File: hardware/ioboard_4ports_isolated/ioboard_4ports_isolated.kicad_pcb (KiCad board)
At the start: 2 copper layers, 106 x 55 mm, 60 parts, among them J1 Conn_02x06_Odd_Even, J10 XLR3, J11 XLR3, J12 Conn_01x03, J13 Conn_01x03, J14 8P8C, J2 XLR3, J3 XLR3, J4 XLR3, J5 XLR3, J6 Conn_01x03, J7 Conn_01x03, J8 XLR3, J9 XLR3, U1 M24C64-RMN6TP, U2 CRE1S0505DC, U3 CRE1S0505DC, U4 ADM2483xRW, U5 ADM2483xRW, U6 ADM2483xRW, U7 ADM2483xRW

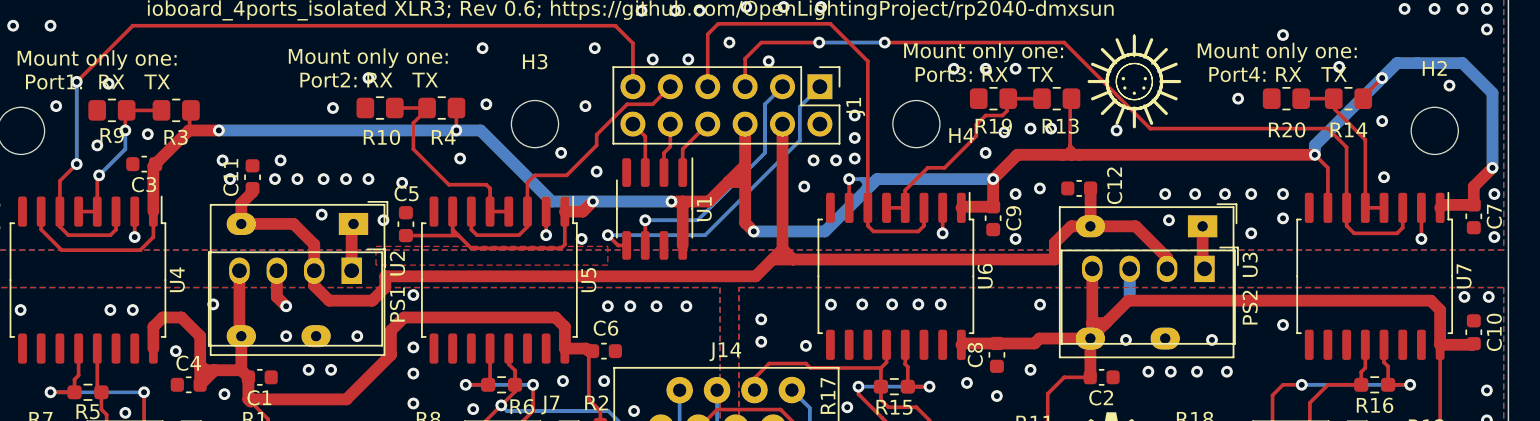
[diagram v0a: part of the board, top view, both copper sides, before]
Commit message: Update all footprints and ignore all other DRC warning on ioboards
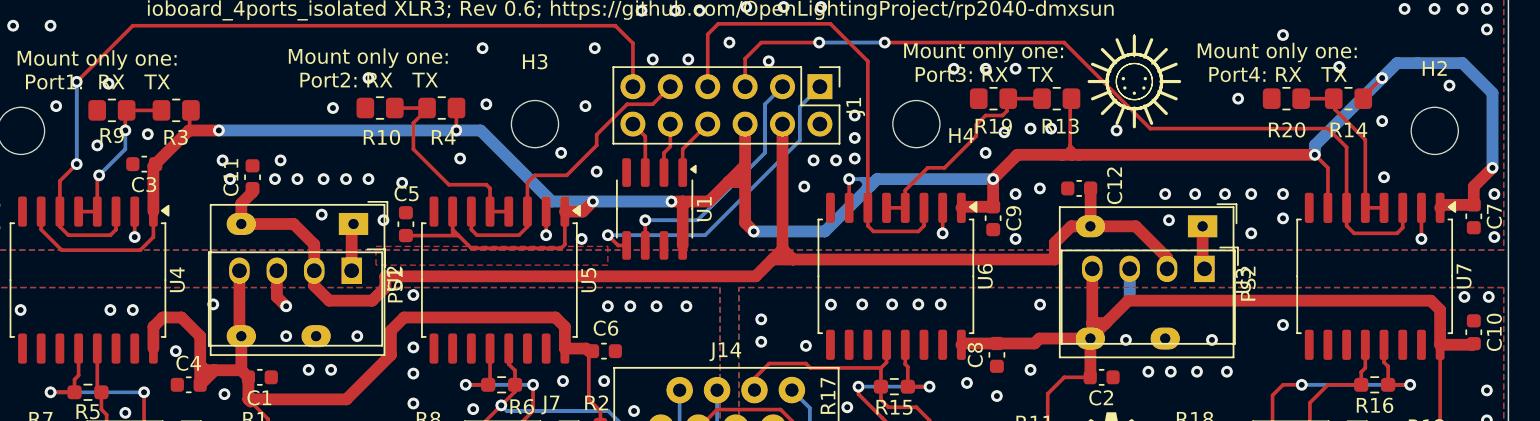
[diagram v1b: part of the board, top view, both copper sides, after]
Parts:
- PS1, PS2: footprint Converter_DCDC:Converter_DCDC_muRata_CRE1xxxxxx3C_THT -> Converter_DCDC:Converter_DCDC_Murata_CRE1xxxxxx3C_THT
- U2, U3: footprint Converter_DCDC:Converter_DCDC_muRata_CRE1xxxxxxDC_THT -> Converter_DCDC:Converter_DCDC_Murata_CRE1xxxxxxDC_THT
